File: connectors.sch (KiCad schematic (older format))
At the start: 7 parts, among them J1 Wuerth_7499010121A, J4 Micro_SD_Card, U2 ET60T-02-24-02-X-RTX-GP

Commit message: updates
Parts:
- removed C17, C18: C_Small, Capacitor_SMD:C_0603_1608Metric, symbol Device:C_Small
- removed J1: Wuerth_7499010121A, Connector_RJ:RJ45_Wuerth_7499010121A_Horizontal, symbol Connector:Wuerth_7499010121A
- removed R3: R_Small, symbol Device:R_Small
- removed R36: R_Small, Resistor_SMD:R_0603_1608Metric, symbol Device:R_Small
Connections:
- net JTAG_TCK: now also U2.20; no longer U2.22
- net JTAG_TDI: now also U2.12; no longer U2.20
- net JTAG_TDO: now also U2.11; no longer U2.19
- net JTAG_TMS: now also U2.19; no longer U2.21
- net RD_N: now also U2.21
- net RD_P: now also U2.22
- net TD_N: now also U2.23
- net TD_P: now also U2.24
- net ~JTAG_TRST: now also U2.13; no longer U2.23
- net ~SYSRESET: now also U2.14; no longer U2.11
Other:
- moved on the sheet: J4, U2A, U2B

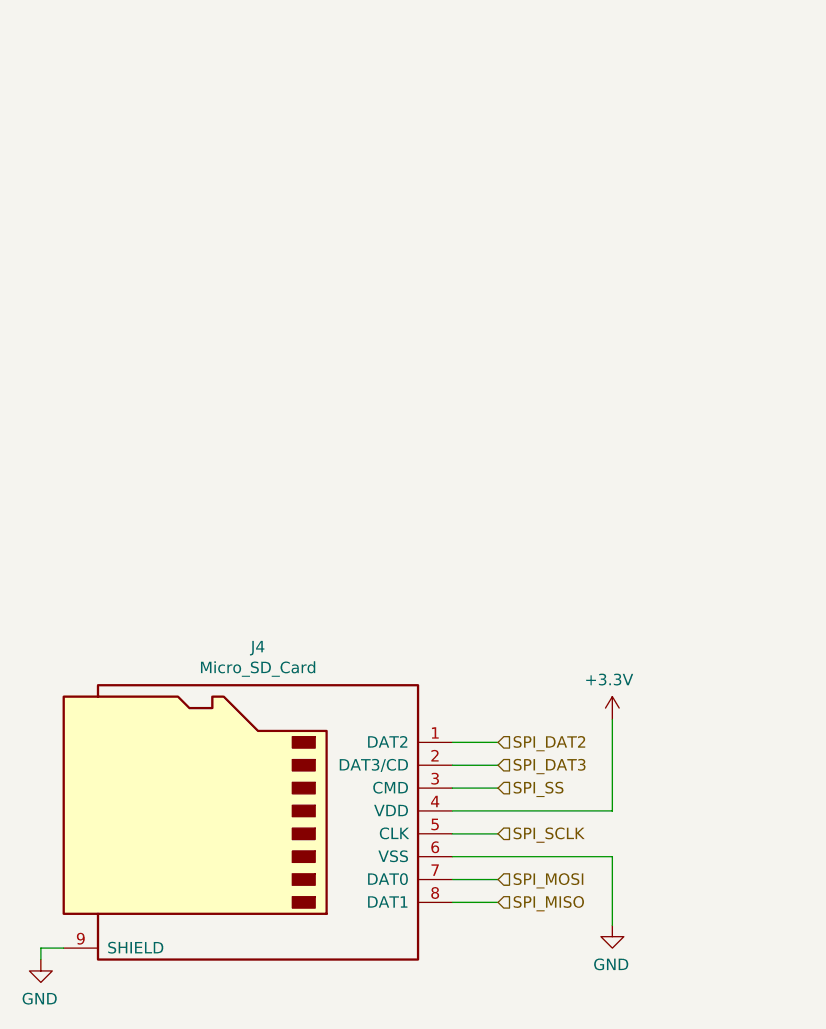
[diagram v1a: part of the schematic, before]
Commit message: fixing some unnamed nets.
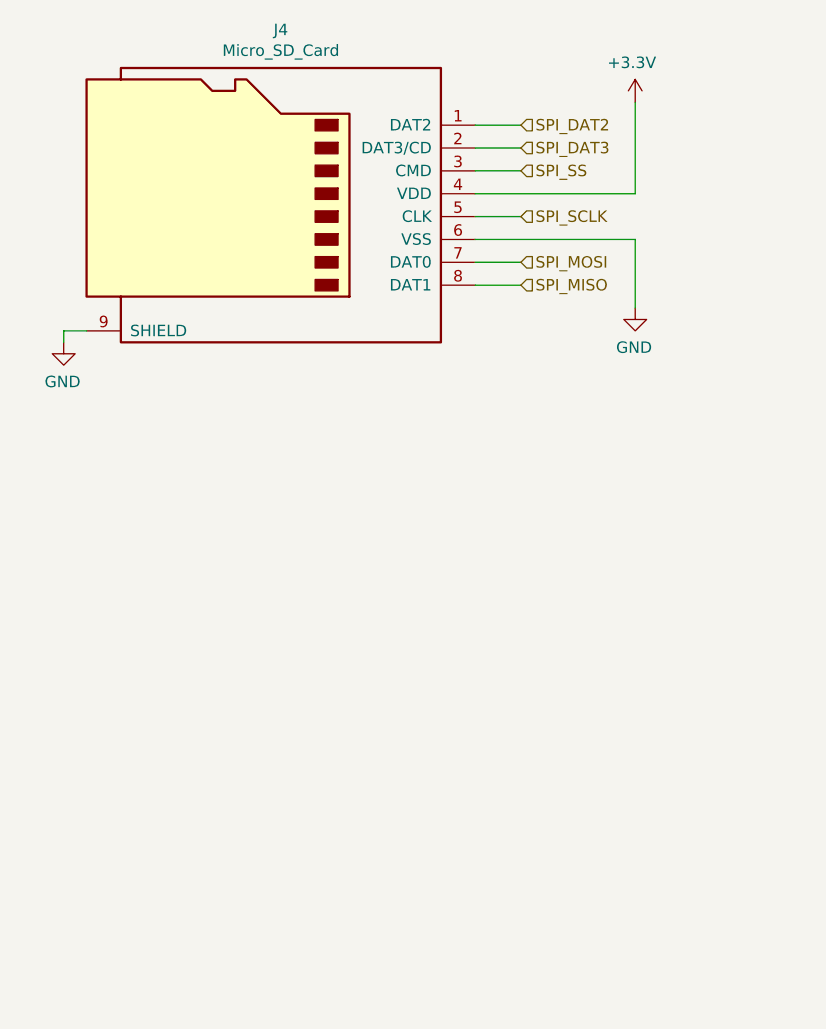
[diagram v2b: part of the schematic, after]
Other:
- moved on the sheet: J4
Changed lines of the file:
@@
 L Connector:Micro_SD_Card J?
 U 1 1 5CA03CFE
-P 2200 4850
+P 2300 2150
 AR Path="/5CA03CFE" Ref="J?"  Part="1"
 AR Path="/5C8128A2/5CA03CFE" Ref="J4"  Part="1"
-F 0 "J4" H 2150 5567 50  0000 C CNN
-F 1 "Micro_SD_Card" H 2150 5476 50  0000 C CNN
-F 2 "Connector_Card:microSD_HC_Wuerth_693072010801" H 3350 5150 50  0001 C CNN
-F 3 "http://katalog.we-online.de/em/datasheet/693072010801.pdf" H 2200 4850 50  0001 C CNN
-	1    2200 4850
+F 0 "J4" H 2250 2867 50  0000 C CNN
+F 1 "Micro_SD_Card" H 2250 2776 50  0000 C CNN
+F 2 "Connector_Card:microSD_HC_Wuerth_693072010801" H 3450 2450 50  0001 C CNN
+F 3 "http://katalog.we-online.de/em/datasheet/693072010801.pdf" H 2300 2150 50  0001 C CNN
+	1    2300 2150
 	-1   0    0    -1
 $EndComp
@@
 L power:GND #PWR0193
 U 1 1 5CA0F158
-P 1300 5500
-F 0 "#PWR0193" H 1300 5250 50  0001 C CNN
-F 1 "GND" H 1305 5327 50  0000 C CNN
-F 2 "" H 1300 5500 50  0001 C CNN
-F 3 "" H 1300 5500 50  0001 C CNN
-	1    1300 5500
+P 1400 2800
+F 0 "#PWR0193" H 1400 2550 50  0001 C CNN
+F 1 "GND" H 1405 2627 50  0000 C CNN
+F 2 "" H 1400 2800 50  0001 C CNN
+F 3 "" H 1400 2800 50  0001 C CNN
+	1    1400 2800
 	-1   0    0    -1
 $EndComp
 Wire Wire Line
-	1400 5450 1300 5450
+	1500 2750 1400 2750
 Wire Wire Line
-	1300 5450 1300 5500
+	1400 2750 1400 2800
 Wire Wire Line
-	3100 4850 3800 4850
+	3200 2150 3900 2150
 Wire Wire Line
-	3800 4850 3800 4450
+	3900 2150 3900 1750
 Wire Wire Line
-	3100 5050 3800 5050
+	3200 2350 3900 2350
 Wire Wire Line
-	3800 5050 3800 5350
+	3900 2350 3900 2650
 $Comp
 L power:GND #PWR0194
 U 1 1 5CA2269B
-P 3800 5350
-F 0 "#PWR0194" H 3800 5100 50  0001 C CNN
-F 1 "GND" H 3805 5177 50  0000 C CNN
-F 2 "" H 3800 5350 50  0001 C CNN
-F 3 "" H 3800 5350 50  0001 C CNN
-	1    3800 5350
+P 3900 2650
+F 0 "#PWR0194" H 3900 2400 50  0001 C CNN
+F 1 "GND" H 3905 2477 50  0000 C CNN
+F 2 "" H 3900 2650 50  0001 C CNN
+F 3 "" H 3900 2650 50  0001 C CNN
+	1    3900 2650
 	-1   0    0    -1
 $EndComp
@@
 L power:+3.3V #PWR0195
 U 1 1 5CA227C4
-P 3800 4450
-F 0 "#PWR0195" H 3800 4300 50  0001 C CNN
-F 1 "+3.3V" H 3815 4623 50  0000 C CNN
-F 2 "" H 3800 4450 50  0001 C CNN
-F 3 "" H 3800 4450 50  0001 C CNN
-	1    3800 4450
+P 3900 1750
+F 0 "#PWR0195" H 3900 1600 50  0001 C CNN
+F 1 "+3.3V" H 3915 1923 50  0000 C CNN
+F 2 "" H 3900 1750 50  0001 C CNN
+F 3 "" H 3900 1750 50  0001 C CNN
+	1    3900 1750
 	-1   0    0    -1
 $EndComp
-Text HLabel 3300 5250 2    50   Input ~ 0
+Text HLabel 3400 2550 2    50   Input ~ 0
 SPI_MISO
-Text HLabel 3300 5150 2    50   Input ~ 0
+Text HLabel 3400 2450 2    50   Input ~ 0
 SPI_MOSI
-Text HLabel 3300 4750 2    50   Input ~ 0
+Text HLabel 3400 2050 2    50   Input ~ 0
 SPI_SS
-Text HLabel 3300 4950 2    50   Input ~ 0
+Text HLabel 3400 2250 2    50   Input ~ 0
 SPI_SCLK
 Wire Wire Line
-	3300 5150 3100 5150
+	3400 2450 3200 2450
 Wire Wire Line
-	3300 5250 3100 5250
+	3400 2550 3200 2550
 Wire Wire Line
-	3300 4950 3100 4950
+	3400 2250 3200 2250
 Wire Wire Line
-	3300 4750 3100 4750
-Text HLabel 3300 4650 2    50   Input ~ 0
+	3400 2050 3200 2050
+Text HLabel 3400 1950 2    50   Input ~ 0
 SPI_DAT3
-Text HLabel 3300 4550 2    50   Input ~ 0
+Text HLabel 3400 1850 2    50   Input ~ 0
 SPI_DAT2
 Wire Wire Line
-	3100 4550 3300 4550
+	3200 1850 3400 1850
 Wire Wire Line
-	3100 4650 3300 4650
+	3200 1950 3400 1950
 Wire Wire Line
 	9550 3700 9600 3700

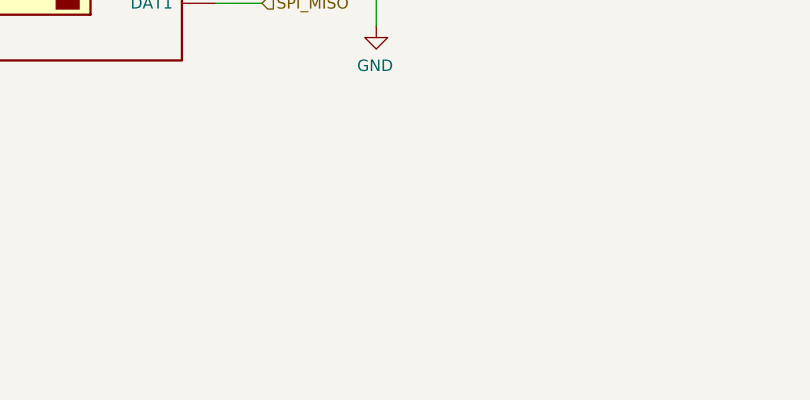
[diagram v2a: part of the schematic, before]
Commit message: Added usb id and usb vbus pins to tm4c circuit. Unconnected on main backplane connector.
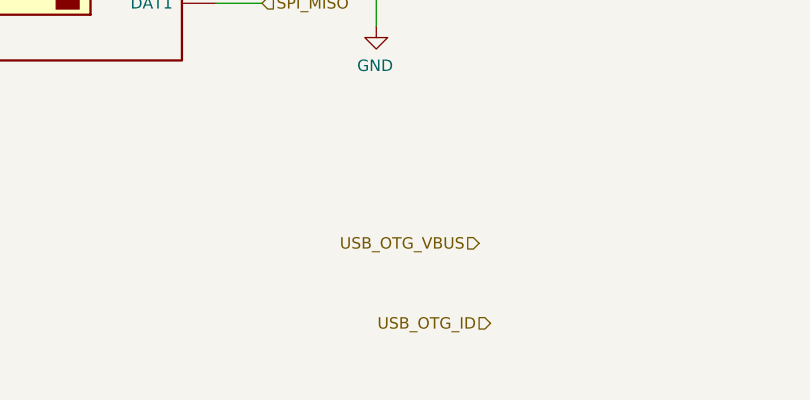
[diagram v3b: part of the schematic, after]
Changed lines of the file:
@@
 Wire Wire Line
 	6550 2700 6700 2700
+Text HLabel 4400 3950 0    50   Input ~ 0
+USB_OTG_ID
+Text HLabel 4350 3600 0    50   Input ~ 0
+USB_OTG_VBUS
 $EndSCHEMATC

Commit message: initial implementation of vbatt for RTC.
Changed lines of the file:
@@
 	3200 2150 3900 2150
-Wire Wire Line
-	3900 2150 3900 1750
 Wire Wire Line
 	3200 2350 3900 2350
@@
 Text HLabel 3400 2450 2    50   Input ~ 0
 SPI_MOSI
-Text HLabel 3400 2050 2    50   Input ~ 0
-SPI_SS
 Text HLabel 3400 2250 2    50   Input ~ 0
 SPI_SCLK
@@
 Wire Wire Line
 	3400 2250 3200 2250
-Wire Wire Line
-	3400 2050 3200 2050
 Text HLabel 3400 1950 2    50   Input ~ 0
 SPI_DAT3
@@
 Text HLabel 4350 3600 0    50   Input ~ 0
 USB_OTG_VBUS
+Wire Wire Line
+	3900 1750 3900 2150
+Text HLabel 3400 2050 2    50   Input ~ 0
+SPI_SS
+Wire Wire Line
+	3200 2050 3400 2050
 $EndSCHEMATC

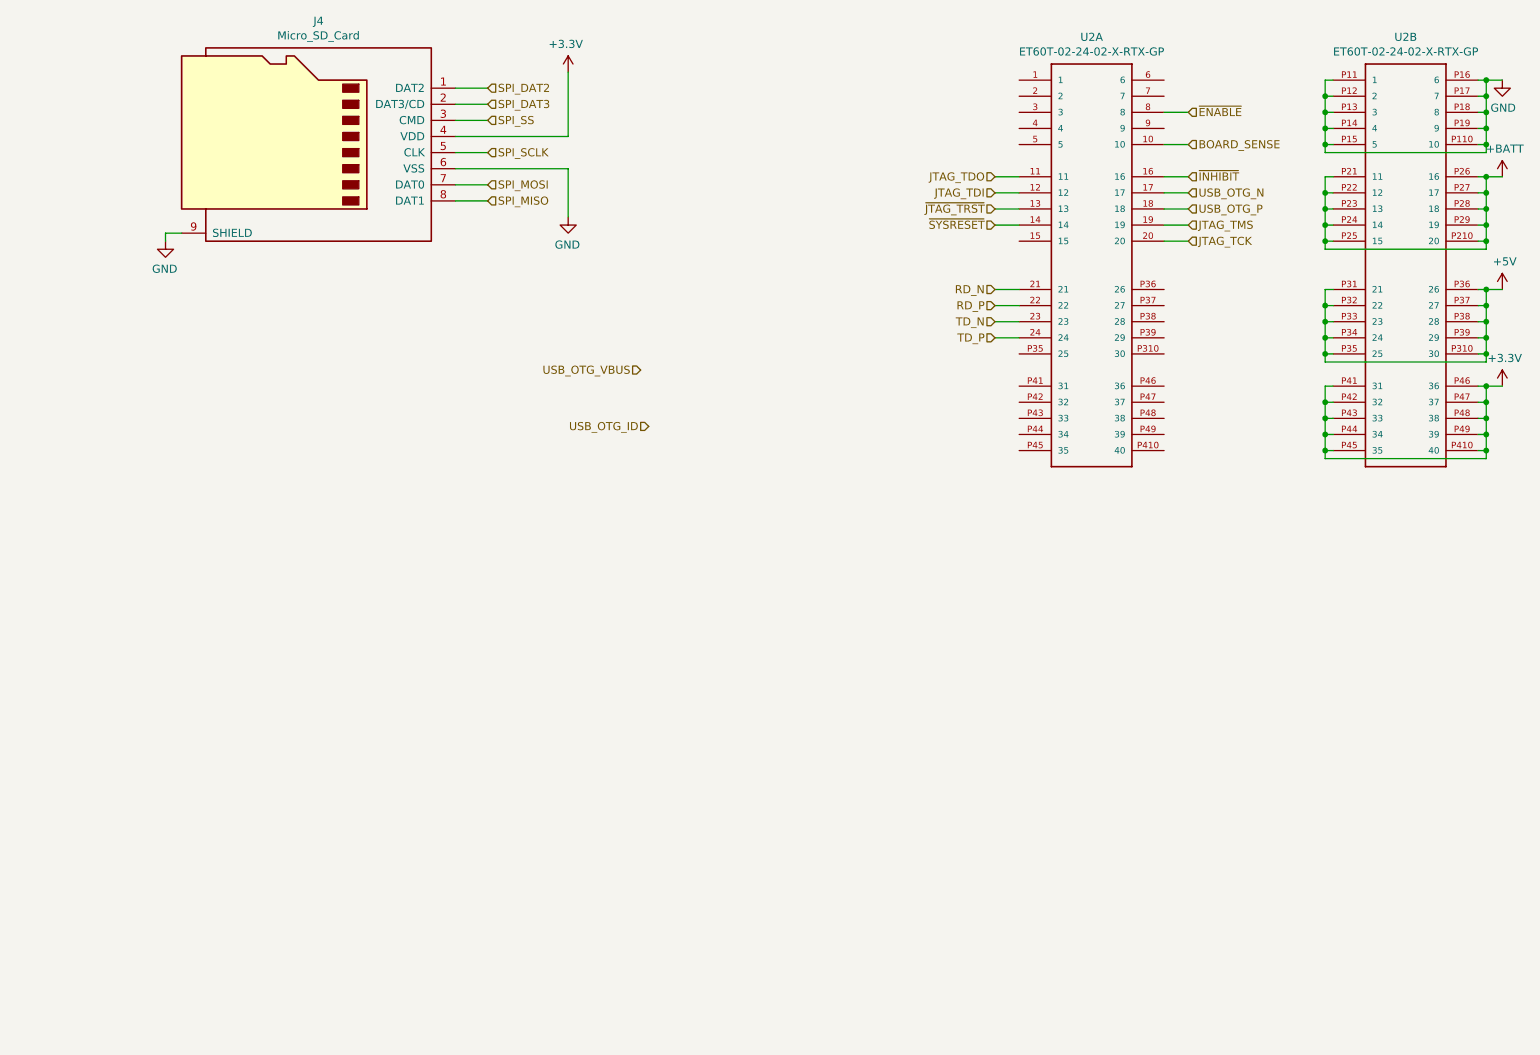
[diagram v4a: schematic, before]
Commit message: added nand flash, removed sd card. finished rtc circuit. added leds
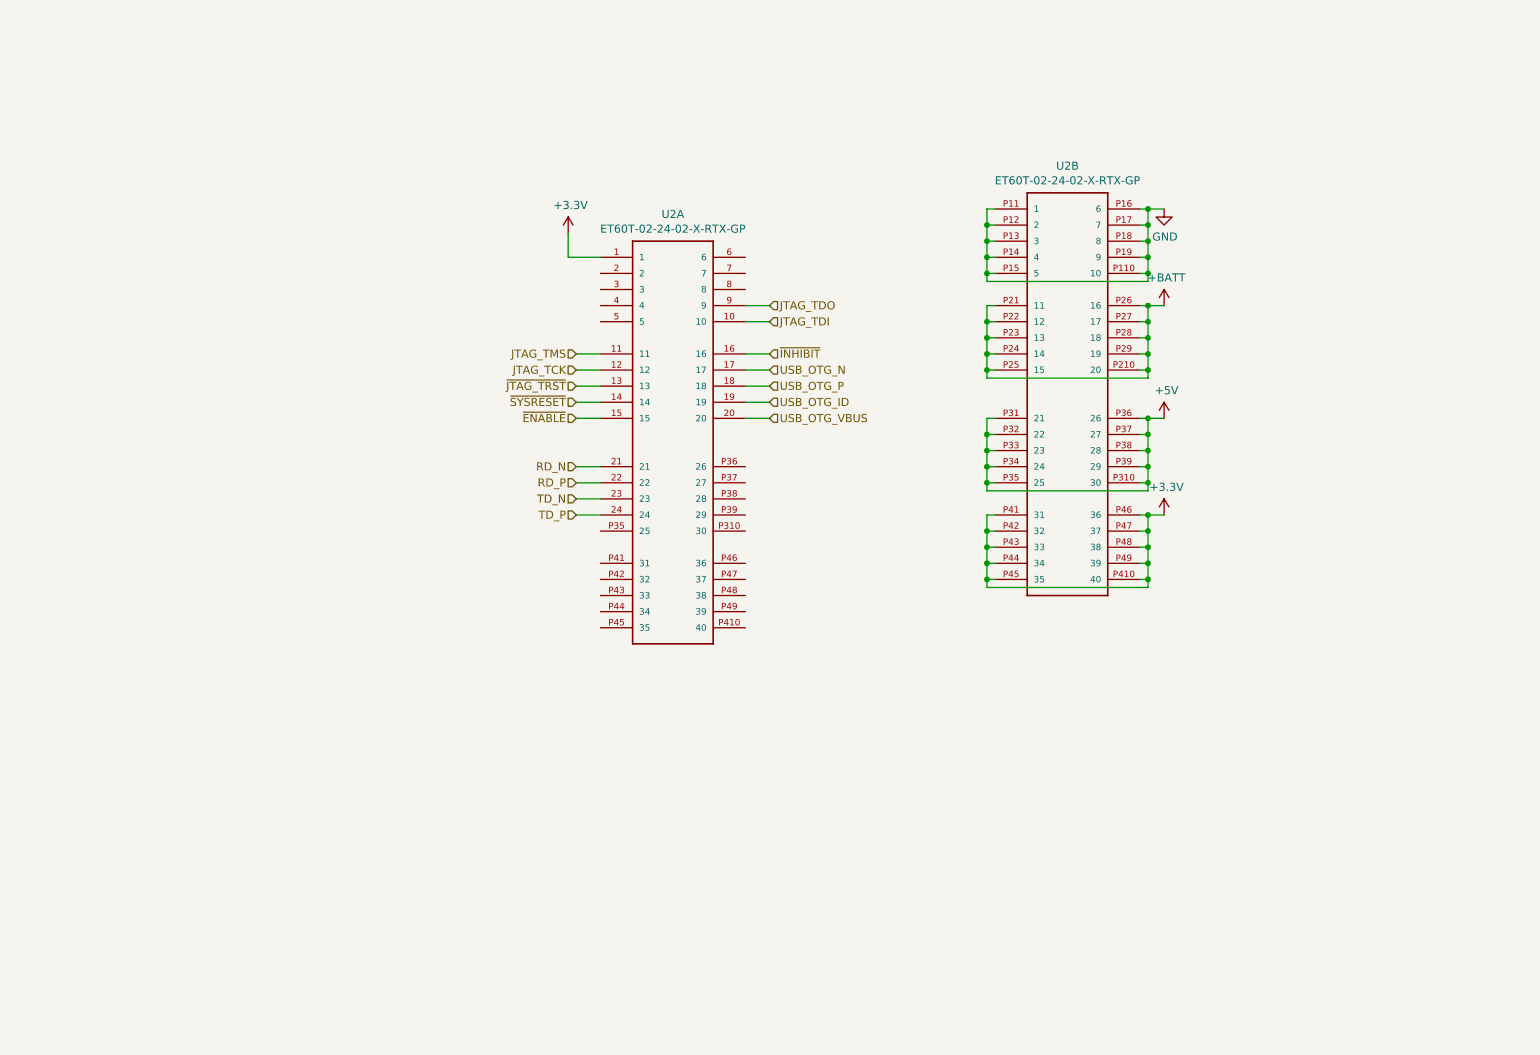
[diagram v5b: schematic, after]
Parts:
- removed J4: Micro_SD_Card, Connector_Card:microSD_HC_Wuerth_693072010801, symbol Connector:Micro_SD_Card
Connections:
- net BOARD_SENSE is gone; now on net JTAG_TDI: U2.10
- net +3V3: now also U2.1
- net JTAG_TCK: now also U2.12; no longer U2.20
- net JTAG_TDI: no longer U2.12
- net JTAG_TDO: now also U2.9; no longer U2.11
- net JTAG_TMS: now also U2.11; no longer U2.19
- net USB_OTG_ID: now also U2.19
- net USB_OTG_VBUS: now also U2.20
- net ~ENABLE: now also U2.15; no longer U2.8
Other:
- moved on the sheet: U2A, U2B

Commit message: Fixed some componenet values. Added some layout notes. added decoupling cap to usb-to-uart circuit.
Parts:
- U2: footprint ET60T-02-24-02-X-RTX-GP -> Exodus_Connectors:ET60T-02-24-02-X-RTX-GP-HS
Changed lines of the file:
@@
 F 0 "U2" H 7000 2867 50  0000 C CNN
 F 1 "ET60T-02-24-02-X-RTX-GP" H 7000 2776 50  0000 C CNN
-F 2 "ET60T-02-24-02-X-RTX-GP" H 6550 2600 50  0001 L BNN
+F 2 "Exodus_Connectors:ET60T-02-24-02-X-RTX-GP-HS" H 6550 2600 50  0001 L BNN
 F 3 "" H 6550 2600 50  0001 L BNN
 F 4 "ET60T-02-24-02-L-RT1-GP" H 6550 2600 50  0001 L BNN "Field4"
@@
 F 0 "U2" H 4550 3167 50  0000 C CNN
 F 1 "ET60T-02-24-02-X-RTX-GP" H 4550 3076 50  0000 C CNN
-F 2 "ET60T-02-24-02-X-RTX-GP" H 4100 2900 50  0001 L BNN
+F 2 "Exodus_Connectors:ET60T-02-24-02-X-RTX-GP-HS" H 4100 2900 50  0001 L BNN
 F 3 "" H 4100 2900 50  0001 L BNN
 F 4 "ET60T-02-24-02-L-RT1-GP" H 4100 2900 50  0001 L BNN "Field4"

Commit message: regenerated netlist/annotations and refdeses. using new connector symbol.
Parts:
- removed U2: ET60T-02-24-02-X-RTX-GP, Exodus_Connectors:ET60T-02-24-02-X-RTX-GP-HS, symbol Exodus_Connectors:ET60T-02-24-02-X-RTX-GP
- added J301: ET60T-000-3-08-D04-x-R1-S-x, Exodus_Connectors:Conn_Samtec_ET60T-000-3-08-D-4-x-R1-S-x, symbol Exodus_Connectors:ET60T-000-3-08-D04-x-R1-S-x
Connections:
- wire segments 106 -> 26
